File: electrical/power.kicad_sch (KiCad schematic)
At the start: 60 parts

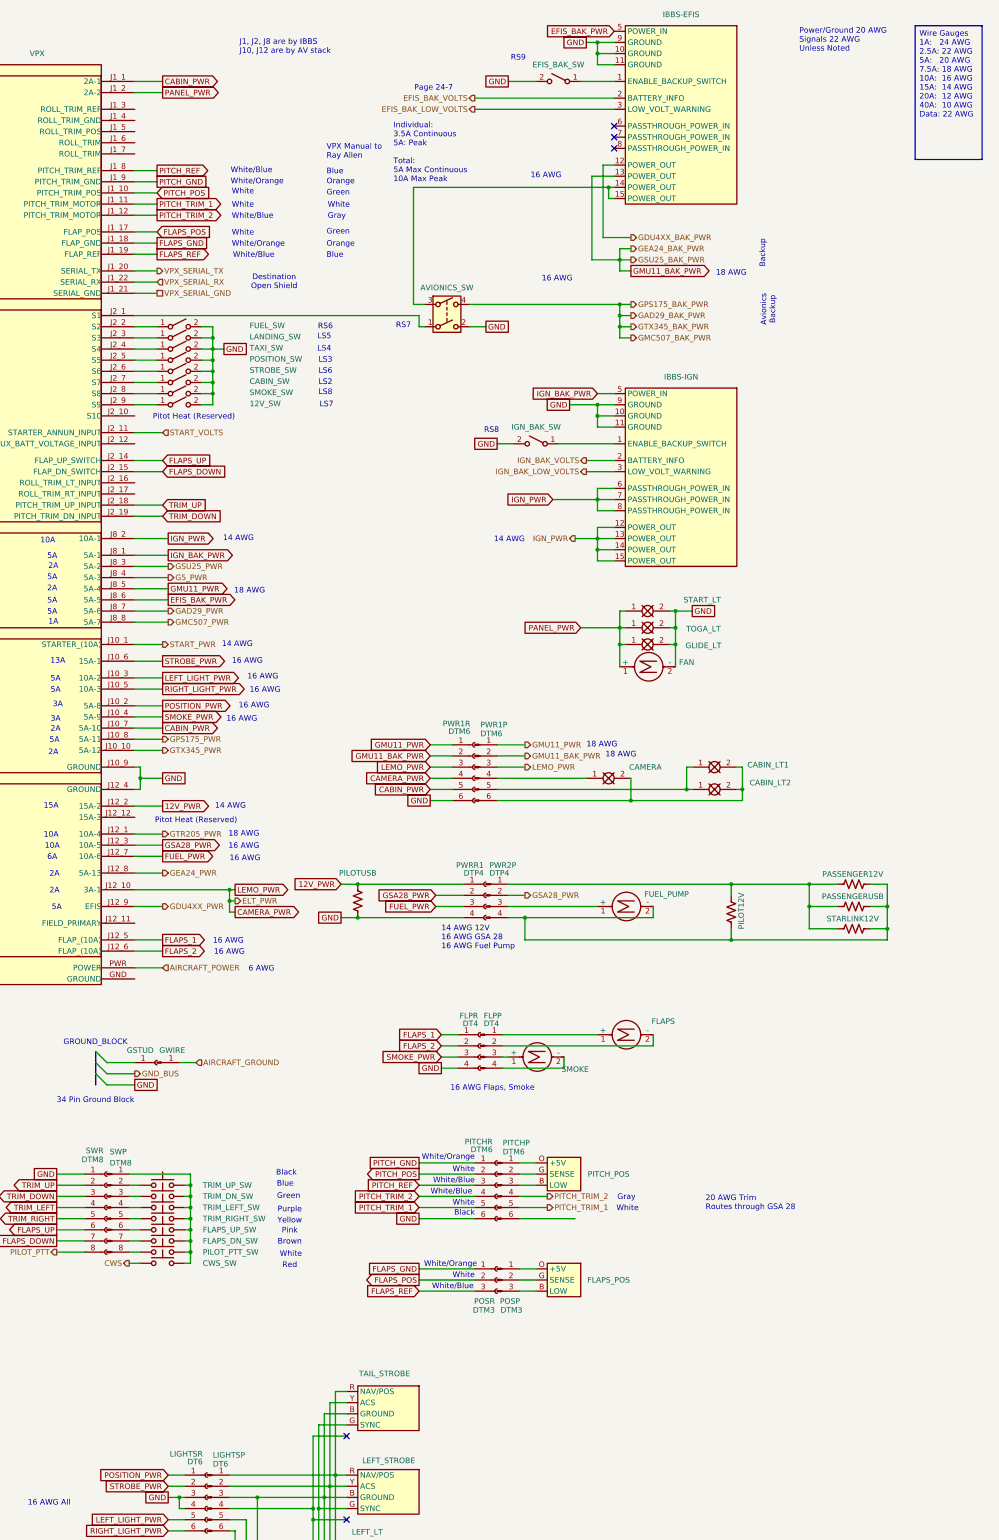
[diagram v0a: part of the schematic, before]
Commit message: Added Field Wire and Alternator symbol.
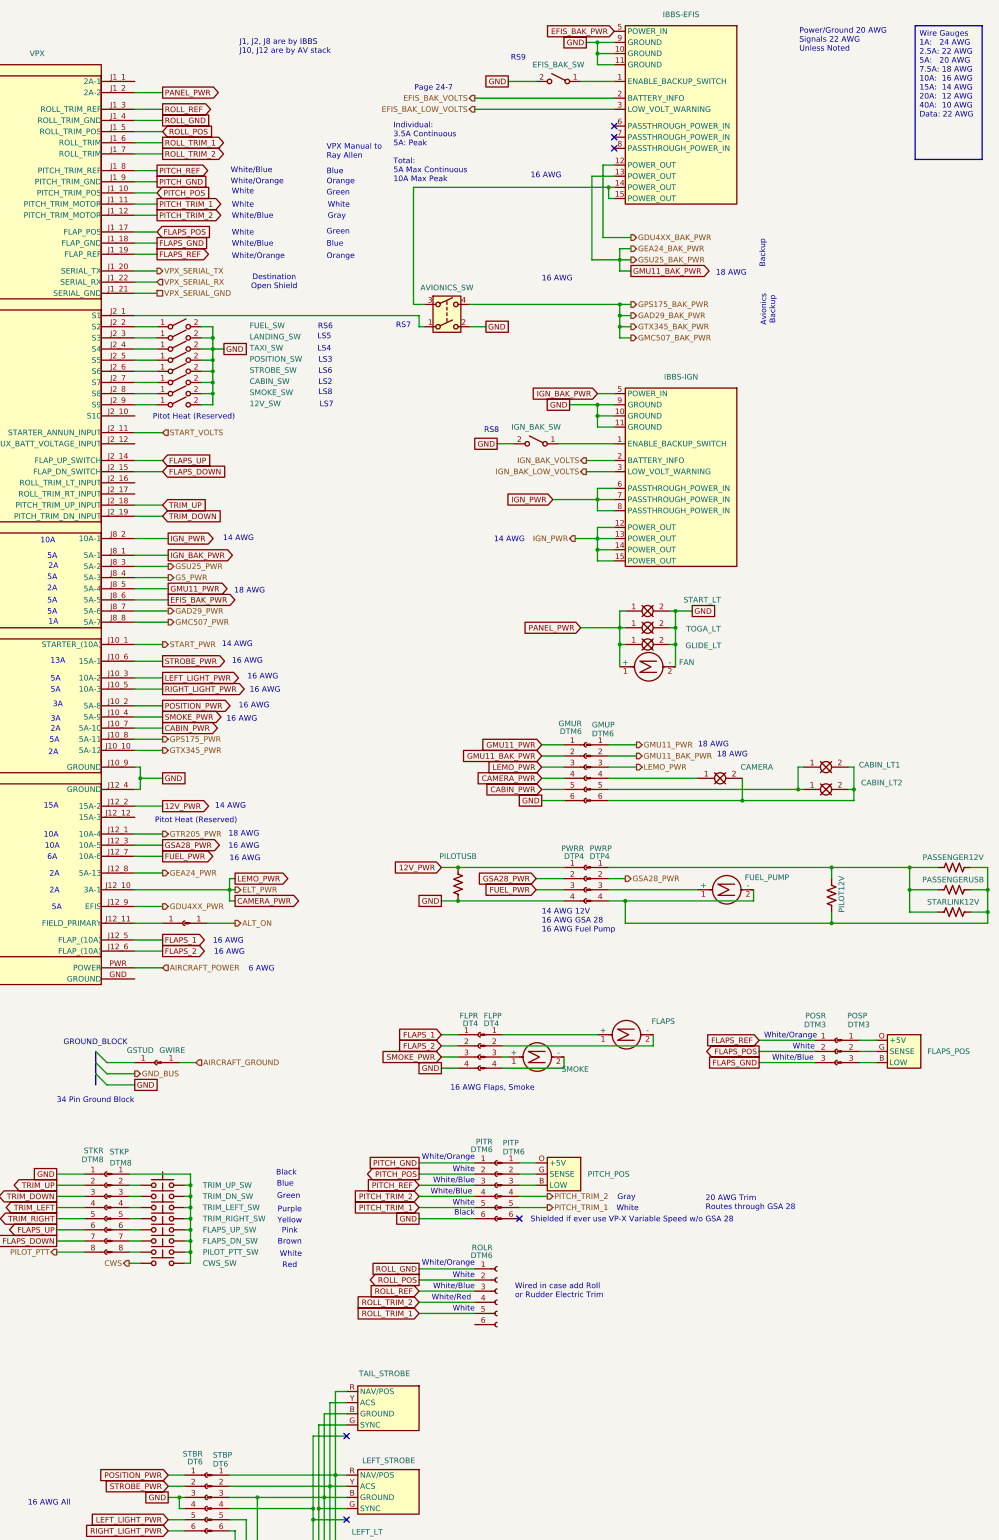
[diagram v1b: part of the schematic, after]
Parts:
- added ALTP: Conn_01x01_Pin, symbol Connector:Conn_01x01_Pin
- added ALTR: Conn_01x01_Socket, symbol Connector:Conn_01x01_Socket
- added ROLR: DTM6, symbol Connector:Conn_01x06_Socket
- renumbered PWR1P to GMUP, PWR1R to GMUR, PITCHP to PITP, PITCHR to PITR, PWR2P to PWRP, PWRR1 to PWRR, LIGHTSP to STBP, LIGHTSR to STBR, SWP to STKP, SWR to STKR
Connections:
- net CABIN_PWR: no longer VPX.J1_1 (2A-1)
- net FLAPS_GND: now also POSR.3 (Pin_3); no longer POSR.1 (Pin_1)
- net FLAPS_REF: now also POSR.1 (Pin_1); no longer POSR.3 (Pin_3)
- net at VPX.J12_11 (FIELD_PRIMARY): now also ALTR.1 (Pin_1)
- net ROLL_REF: now reaches VPX.J1_3 (ROLL_TRIM_REF)
- net ROLL_REF: now also ROLR.3 (Pin_3)
- net ROLL_GND: now reaches VPX.J1_4 (ROLL_TRIM_GND)
- net ROLL_GND: now also ROLR.1 (Pin_1)
- net ROLL_POS: now reaches VPX.J1_5 (ROLL_TRIM_POS)
- net ROLL_POS: now also ROLR.2 (Pin_2)
- net ROLL_TRIM_1: now reaches VPX.J1_6 (ROLL_TRIM)
- net ROLL_TRIM_1: now also ROLR.5 (Pin_5)
- net ROLL_TRIM_2: now reaches VPX.J1_7 (ROLL_TRIM)
- net ROLL_TRIM_2: now also ROLR.4 (Pin_4)
- new net ALT_ON: ALTP.1 (Pin_1)
- no-connect marks 6 -> 7
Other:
- note added: "Shielded if ever use VP-X Variable Speed w/o GSA 28"
- note added: "White/Red"
- note added: "Wired in case add Roll or Rudder Electric Trim"
- moved on the sheet: CABIN_LT1, CABIN_LT2, CAMERA, FLAPS_POS, FUEL_PUMP, GMUP, GMUR, PASSENGER12V, PASSENGERUSB, PILOT12V, PILOTUSB, POSP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

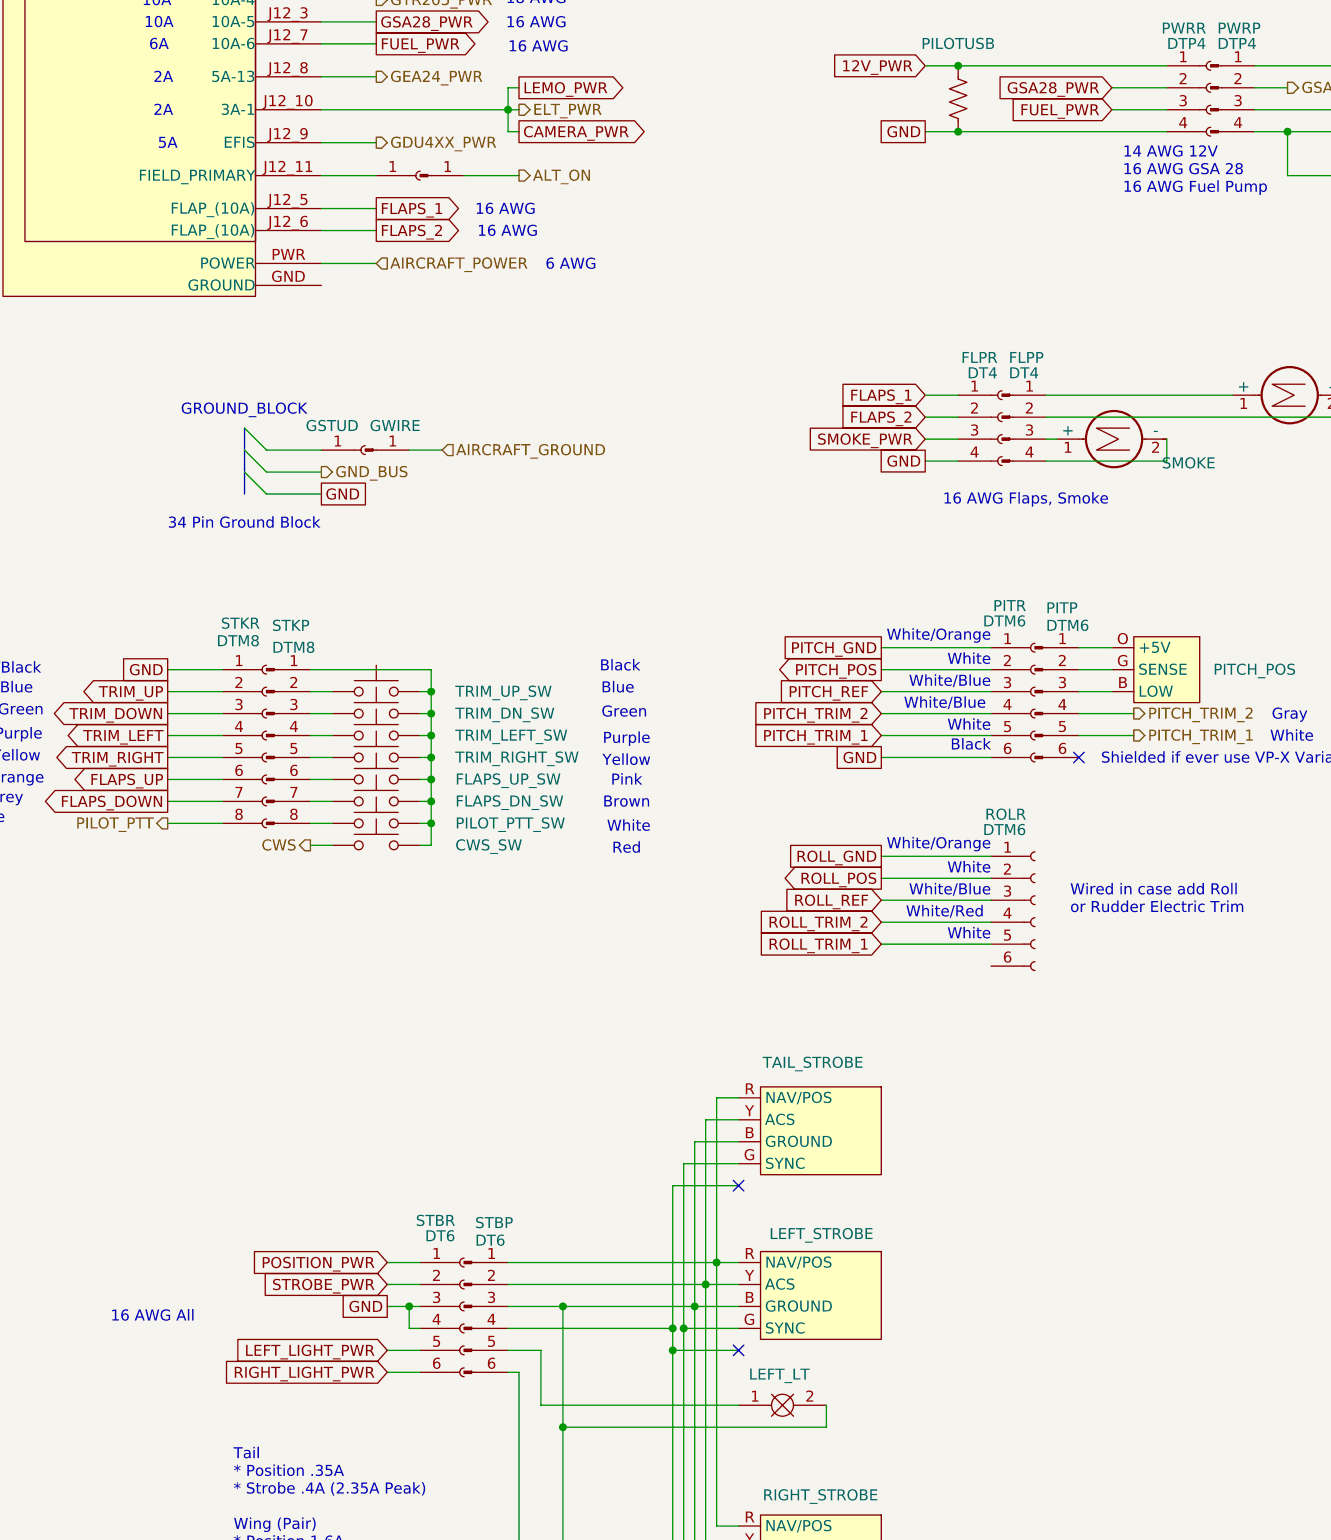
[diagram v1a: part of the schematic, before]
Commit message: Cleaned up ground vs shield markings.
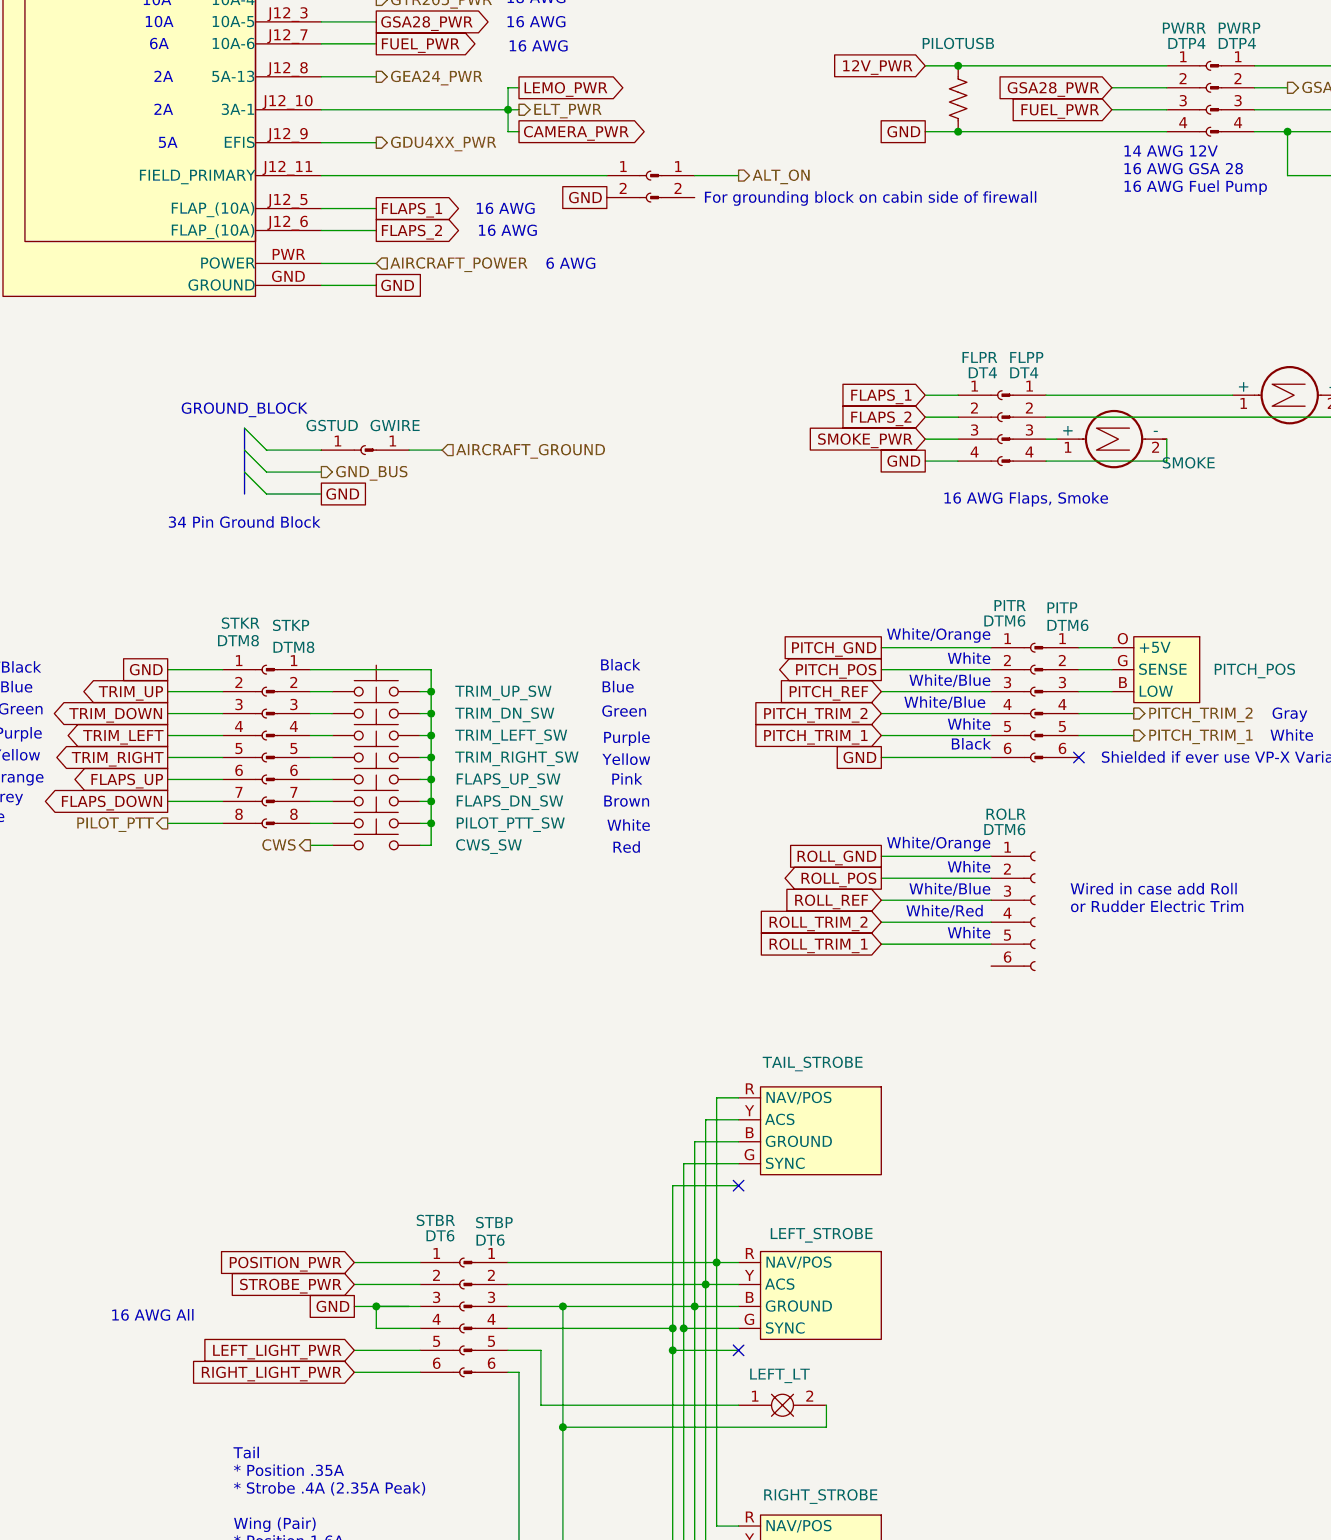
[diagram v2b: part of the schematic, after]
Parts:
- removed ALTP: Conn_01x01_Pin, symbol Connector:Conn_01x01_Pin
- removed ALTR: Conn_01x01_Socket, symbol Connector:Conn_01x01_Socket
- added ALTP: Conn_01x02_Pin, symbol Connector:Conn_01x02_Pin
- added ALTR: Conn_01x02_Socket, symbol Connector:Conn_01x02_Socket
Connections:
- net ALT_ON: now also ALTP.1 (Pin_1)
- net GND: now also VPX.GND (GROUND), ALTR.2 (Pin_2)
- net at VPX.J12_11 (FIELD_PRIMARY): now also ALTR.1 (Pin_1)
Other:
- note added: "For grounding block on cabin side of firewall"

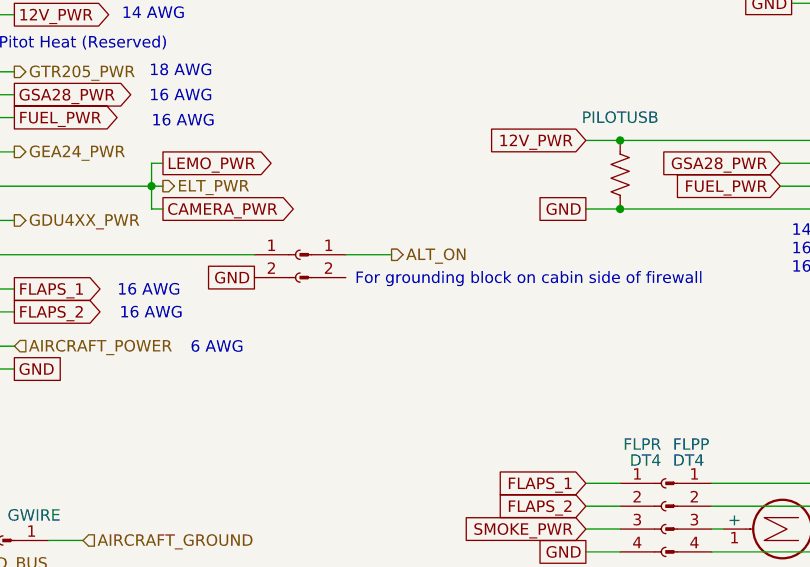
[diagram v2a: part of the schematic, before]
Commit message: Added AWG and connector type to alt on.
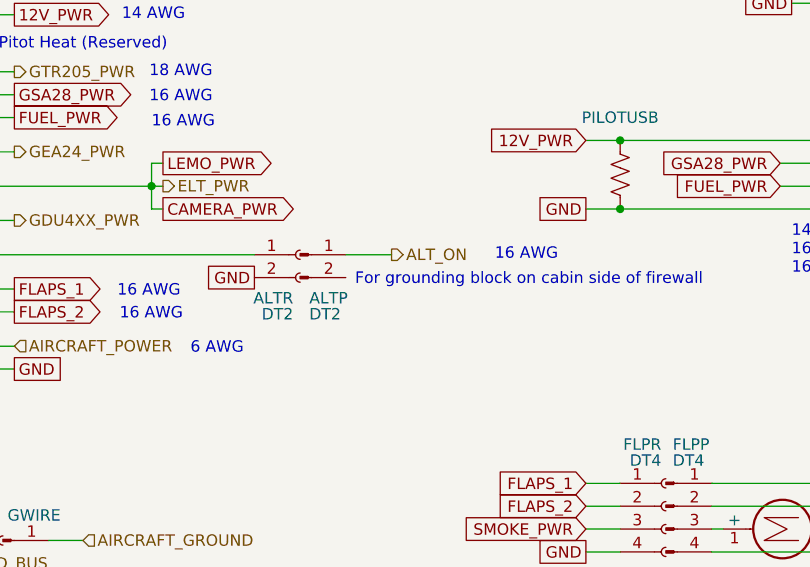
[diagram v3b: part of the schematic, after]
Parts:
- ALTP: value Conn_01x02_Pin -> DT2
- ALTR: value Conn_01x02_Socket -> DT2
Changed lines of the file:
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@@
 		)
 	)
+	(text "16 AWG"
+		(exclude_from_sim no)
+		(at 120.396 220.98 0)
+		(effects
+			(font
+				(size 1.27 1.27)
+			)
+		)
+	)
 	(text "White/Blue"
 		(exclude_from_sim no)
@@
 		(on_board yes)
 		(dnp no)
-		(fields_autoplaced yes)
 		(property "Reference" "ALTP"
-			(at 95.885 215.9 0)
+			(at 96.266 225.806 0)
 			(effects
 				(font
 					(size 1.27 1.27)
 				)
-				(hide yes)
+				(justify left)
 			)
 		)
-		(property "Value" "Conn_01x02_Pin"
-			(at 95.885 218.44 0)
+		(property "Value" "DT2"
+			(at 96.266 227.584 0)
 			(effects
 				(font
 					(size 1.27 1.27)
 				)
-				(hide yes)
+				(justify left)
 			)
 		)
@@
 		(on_board yes)
 		(dnp no)
-		(fields_autoplaced yes)
 		(property "Reference" "ALTR"
-			(at 96.52 220.9799 0)
+			(at 94.488 225.806 0)
 			(effects
 				(font
 					(size 1.27 1.27)
 				)
-				(justify left)
-				(hide yes)
+				(justify right)
 			)
 		)
-		(property "Value" "Conn_01x02_Socket"
-			(at 96.52 223.5199 0)
+		(property "Value" "DT2"
+			(at 94.488 227.584 0)
 			(effects
 				(font
 					(size 1.27 1.27)
 				)
-				(justify left)
-				(hide yes)
+				(justify right)
 			)
 		)

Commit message: Added lighting bus
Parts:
- added LIGHTS_POT: R_Potentiometer_US, symbol Device:R_Potentiometer_US
- added POTP: DTM3P, symbol Connector:Conn_01x03_Pin
- added POTR: DTM3R, symbol Connector:Conn_01x03_Socket
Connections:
- net GND: now also POTR.3 (Pin_3)
- net PANEL_PWR: now also VPX.J1_1 (2A-1), POTR.1 (Pin_1); no longer GLIDE_LT.1, START_LT.1, TOGA_LT.1, VPX.J1_2 (2A-2)
- new net: LIGHTS_POT.1, POTP.1 (Pin_1)
- new net: LIGHTS_POT.2, POTP.2 (Pin_2)
- new net: LIGHTS_POT.3, POTP.3 (Pin_3)
- new net LIGHTS_HI: POTR.2 (Pin_2)
- new net PANEL_LIGHTS_PWR: GLIDE_LT.1, START_LT.1, TOGA_LT.1, VPX.J1_2 (2A-2)
- no-connect marks 7 -> 8
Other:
- note added: "Extra wire originally used for fan. Heatshrinked"
- moved on the sheet: FAN
